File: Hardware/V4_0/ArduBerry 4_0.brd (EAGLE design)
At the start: 50.9 x 60.9 mm, 30 parts, among them J1 AVR_SPI_PRG_62X3_LOCK, J2 POWER_JACKPTH_LOCK, Q3 MOSFET-N-044020001, Q4 MOSFET-N-044020001, U1 ATMEGA328P_PDIP, U2 ARDUINO_SHIELDNO_SILK

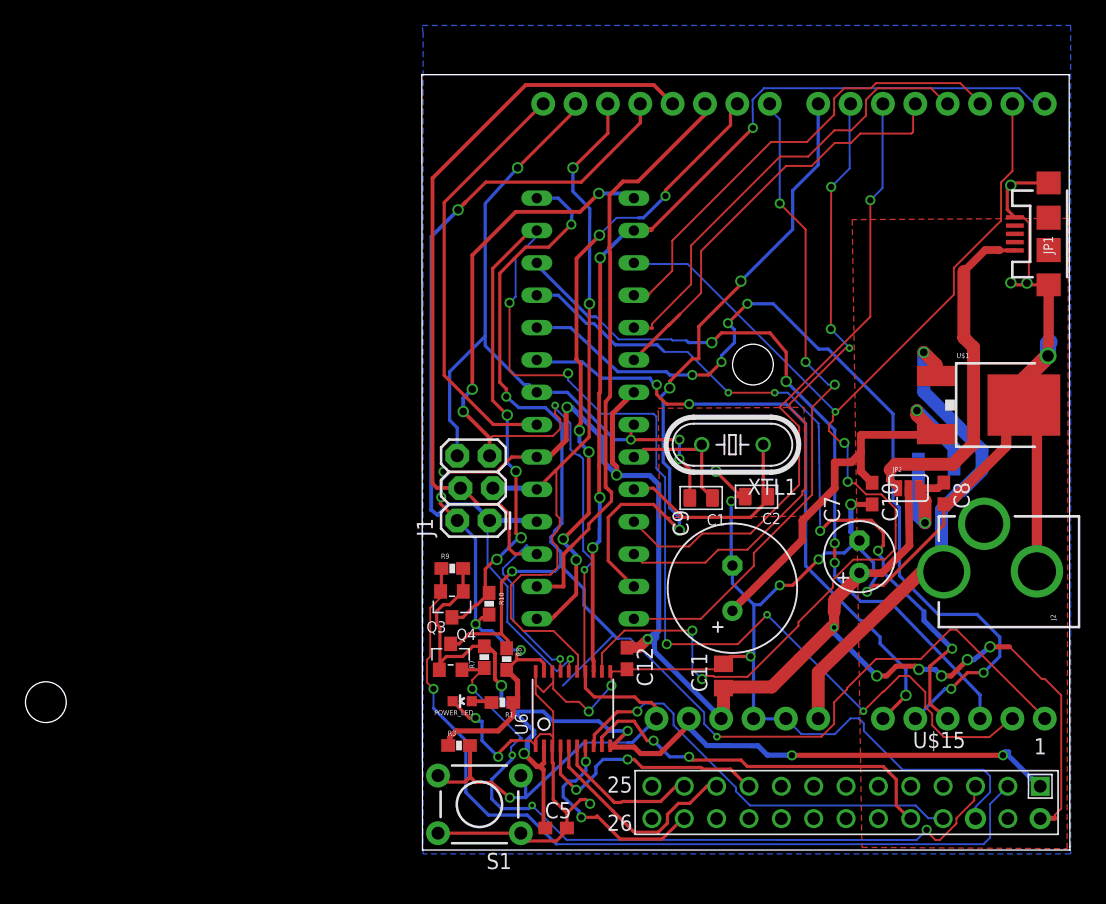
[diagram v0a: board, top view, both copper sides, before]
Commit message: Updated readme and hardware organization
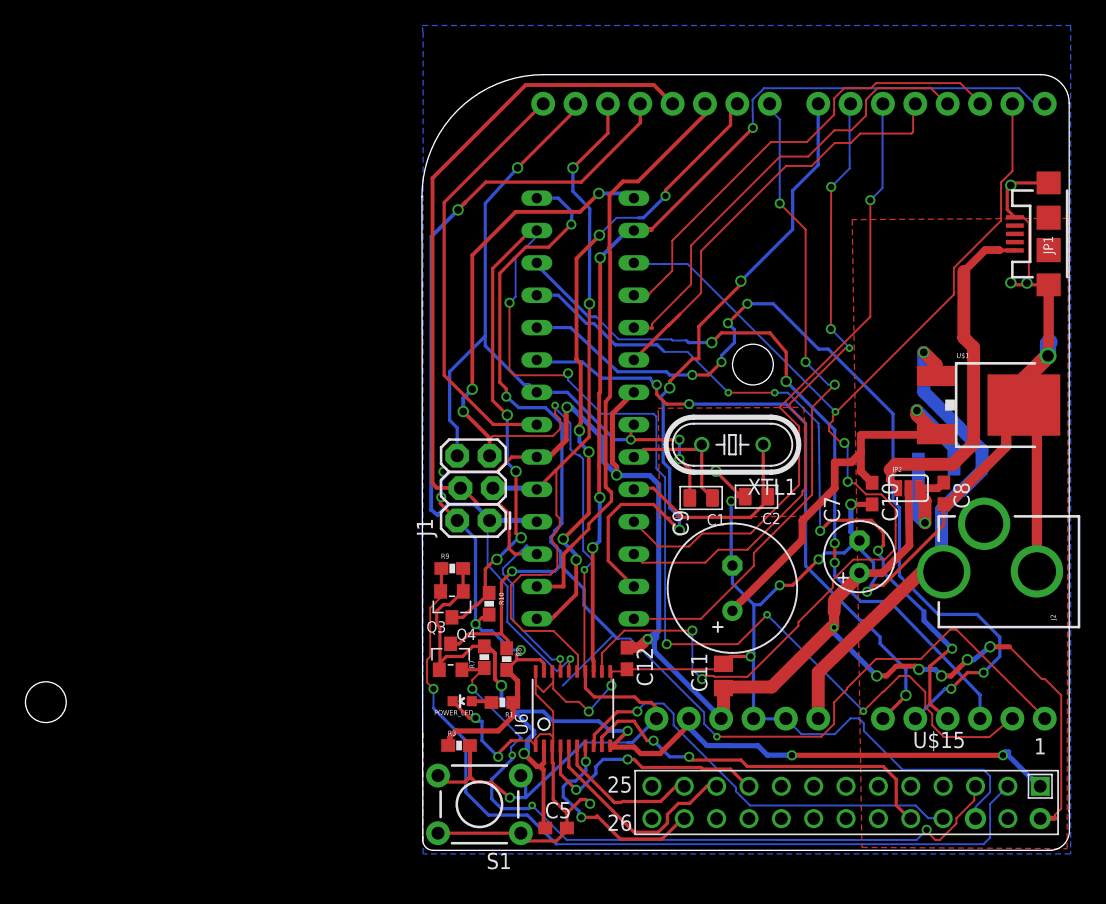
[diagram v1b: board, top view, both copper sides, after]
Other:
- board size 50.9 x 60.9 mm -> 50.8 x 60.9 mm
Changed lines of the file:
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@@
 <setting verticaltext="up"/>
 </settings>
-<grid distance="10" unitdist="mil" unit="mil" style="lines" multiple="1" display="yes" altdistance="0.025" altunitdist="inch" altunit="inch"/>
+<grid distance="1" unitdist="mil" unit="mil" style="lines" multiple="1" display="yes" altdistance="0.025" altunitdist="inch" altunit="inch"/>
 <layers>
 <layer number="1" name="Top" color="4" fill="1" visible="yes" active="yes"/>
@@
 <layer number="17" name="Pads" color="2" fill="1" visible="yes" active="yes"/>
 <layer number="18" name="Vias" color="2" fill="1" visible="yes" active="yes"/>
-<layer number="19" name="Unrouted" color="6" fill="1" visible="no" active="yes"/>
+<layer number="19" name="Unrouted" color="6" fill="1" visible="yes" active="yes"/>
 <layer number="20" name="Dimension" color="15" fill="1" visible="yes" active="yes"/>
 <layer number="21" name="tPlace" color="7" fill="1" visible="yes" active="yes"/>
@@
 <layer number="23" name="tOrigins" color="15" fill="1" visible="yes" active="yes"/>
 <layer number="24" name="bOrigins" color="15" fill="1" visible="yes" active="yes"/>
-<layer number="25" name="tNames" color="7" fill="1" visible="no" active="yes"/>
-<layer number="26" name="bNames" color="7" fill="1" visible="no" active="yes"/>
-<layer number="27" name="tValues" color="7" fill="1" visible="no" active="yes"/>
-<layer number="28" name="bValues" color="7" fill="1" visible="no" active="yes"/>
+<layer number="25" name="tNames" color="7" fill="1" visible="yes" active="yes"/>
+<layer number="26" name="bNames" color="7" fill="1" visible="yes" active="yes"/>
+<layer number="27" name="tValues" color="7" fill="1" visible="yes" active="yes"/>
+<layer number="28" name="bValues" color="7" fill="1" visible="yes" active="yes"/>
 <layer number="29" name="tStop" color="7" fill="3" visible="no" active="yes"/>
 <layer number="30" name="bStop" color="7" fill="6" visible="no" active="yes"/>
@@
 <layer number="116" name="Patch_BOT" color="9" fill="4" visible="no" active="yes"/>
 <layer number="118" name="Rect_Pads" color="7" fill="1" visible="no" active="no"/>
-<layer number="121" name="121bmp" color="14" fill="1" visible="yes" active="yes"/>
+<layer number="121" name="121bmp" color="14" fill="1" visible="no" active="yes"/>
 <layer number="122" name="_bsilk" color="14" fill="1" visible="no" active="yes"/>
 <layer number="123" name="tTestmark" color="7" fill="1" visible="no" active="yes"/>
@@
 <hole x="4.627" y="11.9086" drill="3.2"/>
 <hole x="60.127" y="38.4086" drill="3.2"/>
-<wire x1="34.1884" y1="0.2794" x2="34.1376" y2="61.1646" width="0.0254" layer="20"/>
-<wire x1="34.1376" y1="61.1646" x2="84.9492" y2="61.1646" width="0.0254" layer="20"/>
-<wire x1="84.9492" y1="61.1646" x2="85" y2="0.5588" width="0.0254" layer="20"/>
-<wire x1="85" y1="0.5588" x2="85.0138" y2="0.3032" width="0.0254" layer="20"/>
-<wire x1="85.0138" y1="0.3032" x2="34.174" y2="0.3032" width="0.0254" layer="20"/>
+<wire x1="34.2138" y1="1.2446" x2="34.14660625" y2="51.59174375" width="0.0254" layer="20"/>
+<wire x1="34.14660625" y1="51.59174375" x2="43.7058875" y2="61.1639875" width="0.0254" layer="20" curve="-90.075576"/>
+<wire x1="43.7058875" y1="61.1639875" x2="82.73716875" y2="61.1646" width="0.0254" layer="20"/>
+<wire x1="82.73716875" y1="61.1646" x2="84.951053125" y2="58.953771875" width="0.0254" layer="20" curve="-89.920823"/>
+<wire x1="84.951053125" y1="58.953771875" x2="84.9492" y2="3.3274" width="0.0254" layer="20"/>
+<wire x1="83.2866" y1="0.2778" x2="35.0122" y2="0.2778" width="0.0254" layer="20"/>
 <rectangle x1="76.8731" y1="40.4241" x2="77.6097" y2="40.4495" layer="121" rot="R90"/>
 <rectangle x1="76.8985" y1="41.6941" x2="77.5843" y2="41.7195" layer="121" rot="R90"/>
@@
 <text x="55.626" y="12.192" size="1.016" layer="121" rot="R90">3.3v</text>
 <text x="53.086" y="11.684" size="1.016" layer="121" rot="R90">RESET</text>
+<wire x1="83.2612" y1="0.2794" x2="83.566" y2="0.2794" width="0.0254" layer="20"/>
+<wire x1="83.566" y1="0.2794" x2="84.963" y2="1.9558" width="0.0254" layer="20" curve="90"/>
+<wire x1="84.963" y1="1.9558" x2="84.963" y2="3.4036" width="0.0254" layer="20"/>
+<wire x1="34.2138" y1="1.3462" x2="34.2138" y2="1.0922" width="0.0254" layer="20"/>
+<wire x1="34.2138" y1="1.0922" x2="35.0266" y2="0.2794" width="0.0254" layer="20" curve="90"/>
 </plain>
 <attributes>
@@
 <autorouter>
 <pass name="Default">
-<param name="RoutingGrid" value="3.93700787mil"/>
+<param name="RoutingGrid" value="0.1mm"/>
 <param name="tpViaShape" value="round"/>
 <param name="PrefDir.1" value="/"/>
